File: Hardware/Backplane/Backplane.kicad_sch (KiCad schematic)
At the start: 3 parts, among them J101 10018784-10201TLF

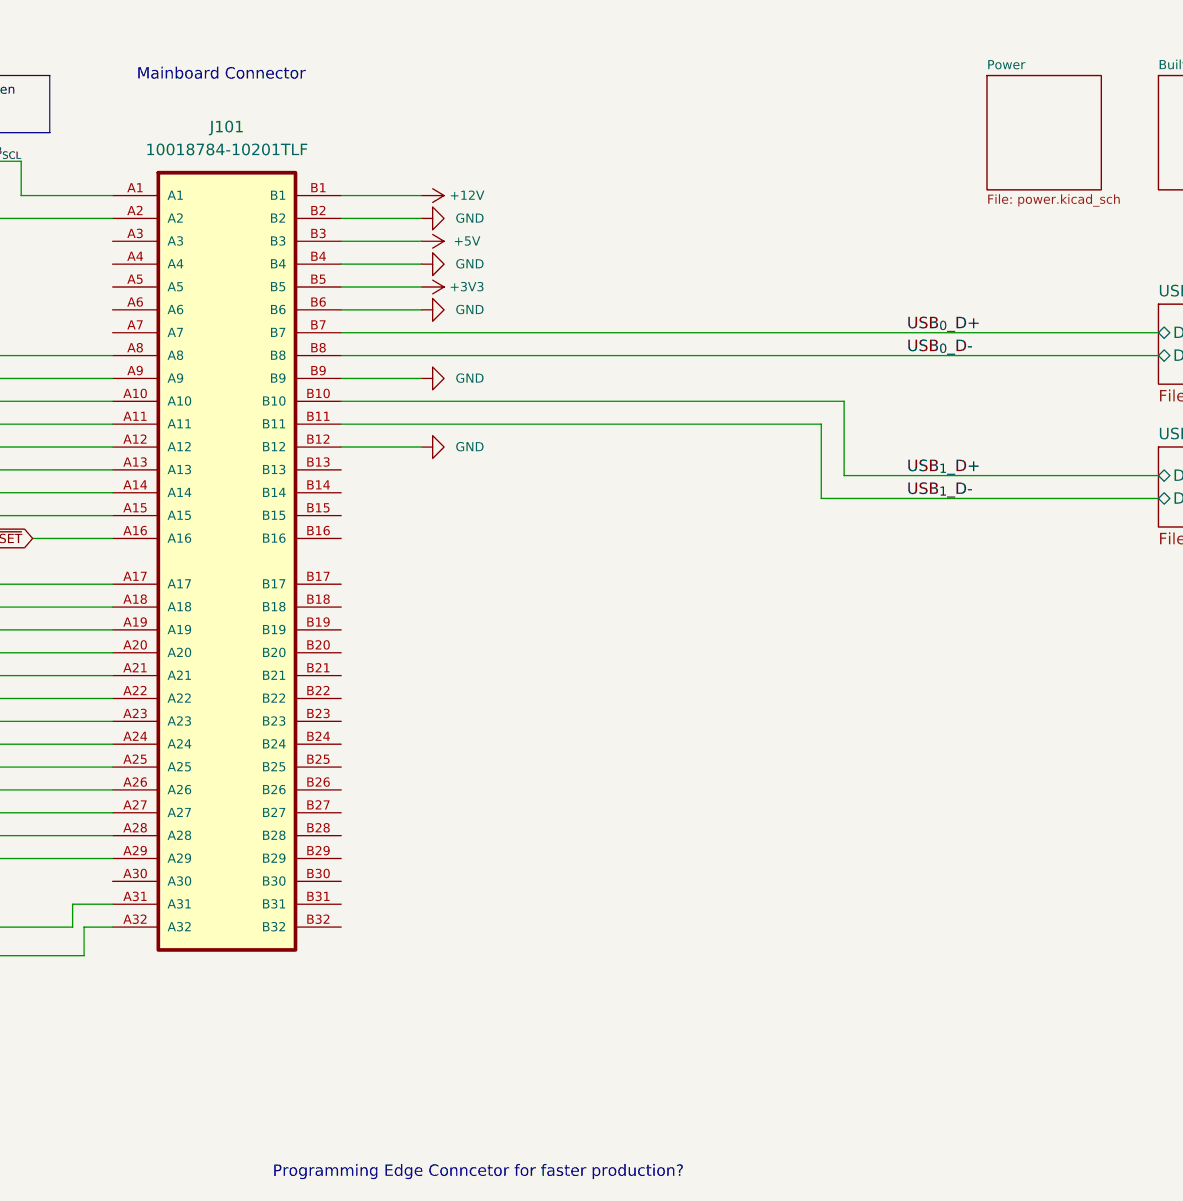
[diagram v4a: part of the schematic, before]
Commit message: More BOM consolidation
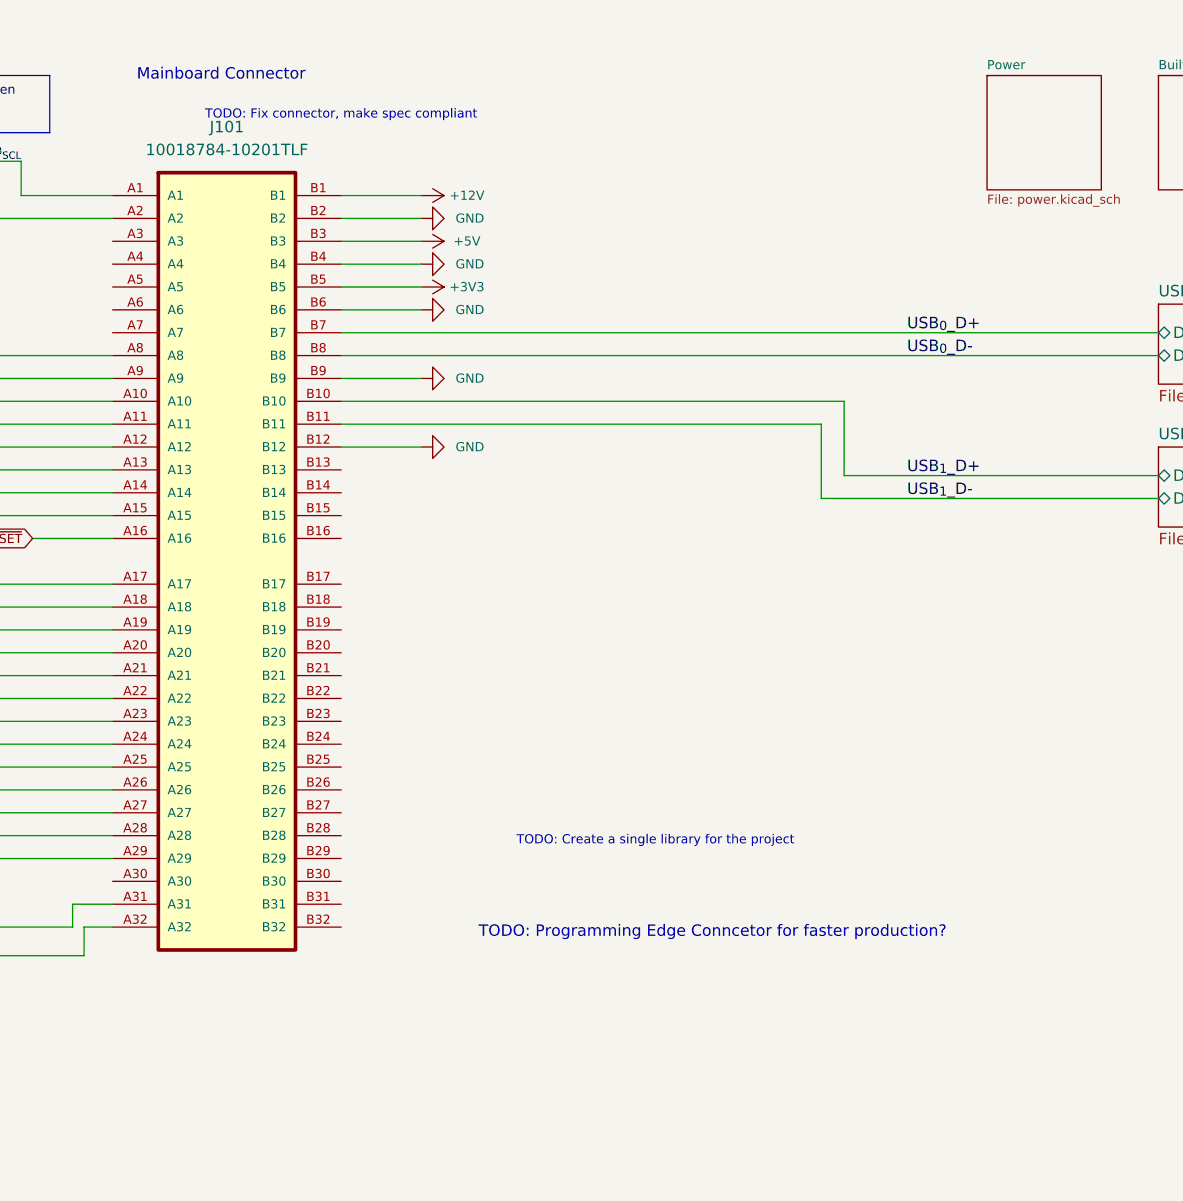
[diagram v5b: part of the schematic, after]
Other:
- note added: "TODO: Create a single library for the project"
- note added: "TODO: Fix connector, make spec compliant"
- note added: "TODO: Programming Edge Conncetor for faster production?"
- note removed: "Programming Edge Conncetor for faster production?"
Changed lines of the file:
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@@
 		)
 	)
-	(text "Programming Edge Conncetor for faster production?\n"
+	(text "TODO: Programming Edge Conncetor for faster production?\n"
 		(exclude_from_sim no)
-		(at 159.385 140.97 0)
+		(at 185.42 114.3 0)
 		(effects
 			(font
@@
 			)
 		)
+	)
+	(text "TODO: Create a single library for the project"
+		(exclude_from_sim no)
+		(at 179.07 104.14 0)
+		(effects
+			(font
+				(size 1.016 1.016)
+			)
+		)
+	)
+	(text "TODO: Fix connector, make spec compliant"
+		(exclude_from_sim no)
+		(at 144.145 23.495 0)
+		(effects
+			(font
+				(size 1.016 1.016)
+			)
+		)

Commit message: Further backplane PCB cleanup.
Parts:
- removed J101: 10018784-10201TLF, Home Computer:CONN_10018784-10201TLF, symbol Home Computer:10018784-10201TLF
- added D1006: GREEN, LED_SMD:LED_0603_1608Metric, symbol LED:LD271
- added J1: 10018784-10201TLF, Home Computer:CONN_10018784-10201TLF, symbol Home Computer:AHC-CONN-CPU
- added R1012: 560, Resistor_SMD:R_0603_1608Metric, symbol Device:R
- added R421, R422, R423, R424: 0, Resistor_SMD:R_0603_1608Metric, symbol Device:R_Small
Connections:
- net +12V: now also J1.A2 (+12V), J1.B2 (+12V)
- net +3V3: now also D1006.2 (A), J1.A4 (+3V3), J1.B4 (+3V3)
- net +5V: now also J1.A3 (+5V), J1.B3 (+5V)
- net Expansions/FAB_~{RES}: now also J1.A8 (~{FAB_RESET})
- net Expansions/HSTX_{0}: now also J1.A13 (HSTX0)
- net Expansions/HSTX_{1}: now also J1.A14 (HSTX1)
- net Expansions/HSTX_{2}: now also J1.A16 (HSTX2)
- net Expansions/HSTX_{3}: now also J1.A17 (HSTX3)
- net Expansions/HSTX_{4}: now also J1.A19 (HSTX4)
- net Expansions/HSTX_{5}: now also J1.A20 (HSTX5)
- net Expansions/HSTX_{6}: now also J1.A22 (HSTX6)
- net Expansions/HSTX_{7}: now also J1.A23 (HSTX7)
- net Expansions/I2S_{BCLK}: now also J1.A28 (I2S_BCLK)
- net Expansions/I2S_{LRCLK}: now also J1.A29 (I2S_WCLK)
- net Expansions/I2S_{MCLK}: now also J1.A31 (I2S_MCLK)
- net Expansions/I2S_{SDI}: now also J1.A25 (I2S_SDIN)
- net Expansions/I2S_{SDO}: now also J1.A26 (I2S_SDOUT)
- net Expansions/MAIN_CLK: now also J1.A11 (CLK)
- net GND: now also J1.A1 (GND), J1.A10 (GND), J1.A12 (GND), J1.A15 (GND), J1.A18 (GND), J1.A21 (GND), J1.A24 (GND), J1.A27 (GND), J1.A30 (GND), J1.A32 (GND), J1.A5 (GND), J1.B11 (GND), J1.B12 (GND), J1.B15 (GND), J1.B18 (GND), J1.B21 (GND), J1.B24 (GND), J1.B27 (GND), J1.B30 (GND), J1.B32 (GND), J1.B5 (GND), R421.2, R422.2, R423.2, R424.2
- net I2C^{FAB}_{SCL}: now also J1.A6 (I2C_SCL)
- net I2C^{FAB}_{SDA}: now also J1.A7 (I2C_SDA)
- net USB_{0}_D+: now also J1.B25 (USB0_D+)
- net USB_{0}_D-: now also J1.B26 (USB0_D-)
- net USB_{1}_D+: now also J1.B28 (USB1_D+)
- net USB_{1}_D-: now also J1.B29 (USB1_D-)
- net ~{RESET}: now also J1.A9 (~{RESET})
- new net: J1.B10 (~{PRESENT}), R1012.2
- new net: J1.B6 (~{SLOT_AUDIO}), R421.1
- new net: J1.B7 (~{SLOT_VIDEO}), R422.1
- new net: J1.B8 (~{SLOT_USB0}), R423.1
- new net: J1.B9 (~{SLOT_USB1}), R424.1
- new net: D1006.1 (K), R1012.1
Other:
- note added: "Mainboard present"
- note added: "default low, must be high for operation"
- note removed: "TODO: Fix connector, make spec compliant"
- moved on the sheet: R102, R103
